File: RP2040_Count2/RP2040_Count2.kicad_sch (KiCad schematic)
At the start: 17 parts, among them J2 String1, J3 OLED, SW1 Test, U2 AMS1117-5.0, U2 rp2040-zero, U4 74AHCT1G125, U4 INA219BxD

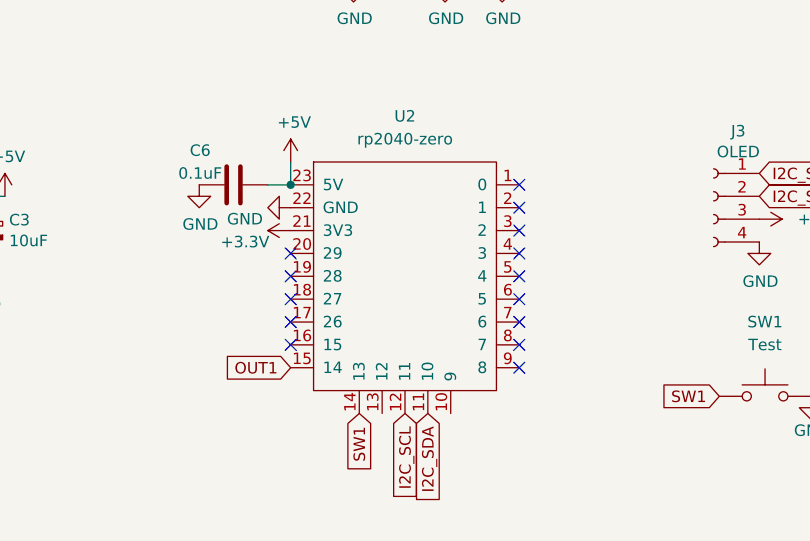
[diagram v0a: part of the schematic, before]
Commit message: add plug in 3 to 4 adapter
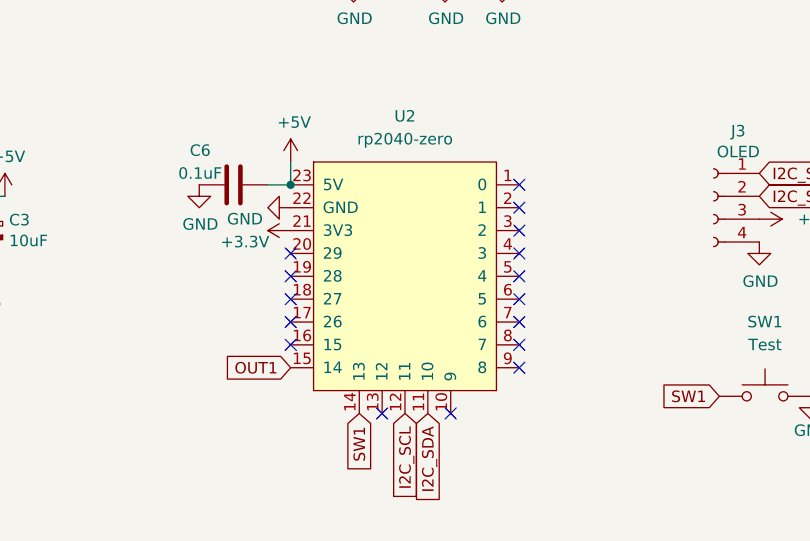
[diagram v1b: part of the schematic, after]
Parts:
- J3: footprint Scotts:OLED-SSD1306-128X64-I2C-THT_2HOLE -> Scotts:OLED-SSD1306-128X64-I2C-THT_SCOTT2
- U4: LCSC PN C87469 -> C138706
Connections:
- no-connect marks 14 -> 16
